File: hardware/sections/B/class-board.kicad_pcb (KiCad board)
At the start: 4 copper layers, 180 x 100 mm, 334 parts, among them J1 DevKit J1 (left row), J10 C2937625_-_Conn_01x03, J11 C2937625_-_Conn_01x03, J12 C2937625_-_Conn_01x03, J13 C492401-PZ254V-11-02P, J14 C2937625_-_Conn_01x03, J15 C2937625_-_Conn_01x03, J2 DevKit J3 (right row), J201 USB-C 16P, J202 DC005-T20, J3 C2937625_-_Conn_01x03, J4 Qwiic, J5 Expansion 2x10, J6 Panel link 2x20 female, J7 Panel link 2x20 female, J8 Panel link 2x20 female, J9 C2937625_-_Conn_01x03, J901 KF301-5.0-2P, J903 KF301-5.0-2P, J905 KF301-5.0-3P, Q901 AOD4185, Q904 AOD4184A, U101 ADS8688IDBTR, U201 LM66100DCKR, U202 LM66100DCKR, U203 78L05G-AB3-R, U204 AMS1117-3.3, U301 DAC8563SDGSR, U302 74HCT125PW, U303 OPA2192IDR, U501 SN74AHCT541PWR, U502 74HCT125PW, U503 SN74LVC1T45DBVR, U505 TCA9535PWR, U701 SI5351A-B-GT, U702 74HC74D,653, U703 OPA1656IDR, U704 DG419DY-T1-E3, U705 OPA1612AIDR, U706 OPA1612AIDR, U801 AD9834BRUZ, U802 OPA564AIDWPR, U901 TS5A23157DGSR, U902 TS5A23157DGSR, U903 DRV8871DDAR, U904 UCC27517DBVR, Y701 25 MHz

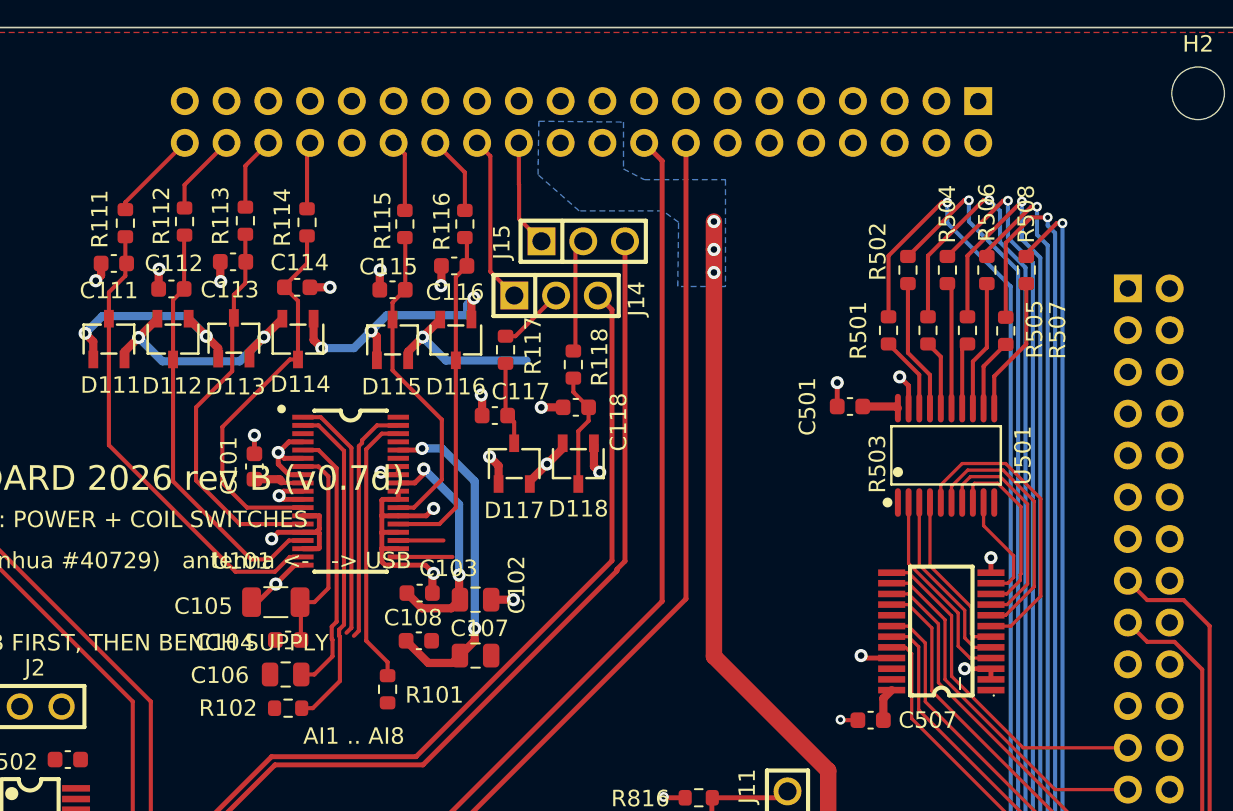
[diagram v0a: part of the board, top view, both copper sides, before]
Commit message: Merge student A (Renqian): area A of the main board (417 tracks/vias, unconnected 197 -> 148) and panel section A (13 analog nets, 121 unconnected left) accepted into the masters; sections re-split
Co-Authored-By: Claude Fable 5.1 <noreply@anthropic.com>
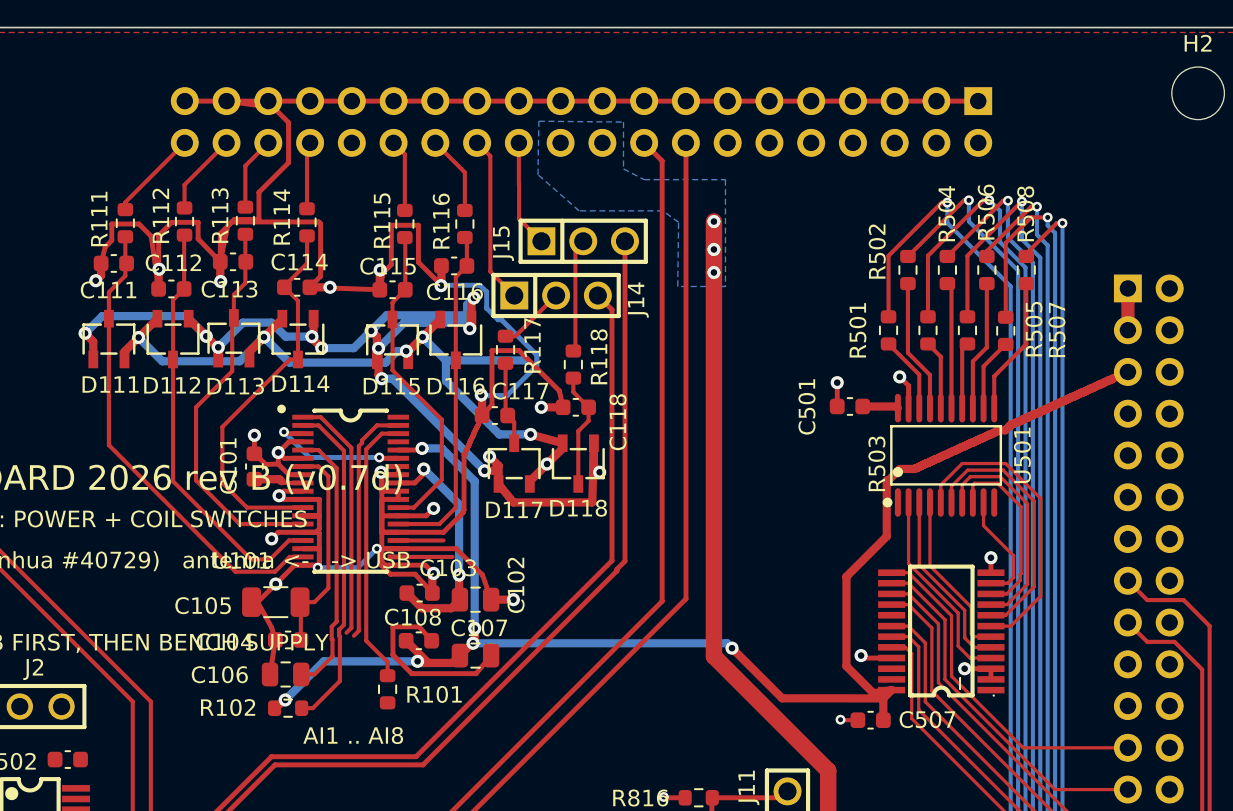
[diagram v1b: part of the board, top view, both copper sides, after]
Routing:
- net AGND: track 162.8 -> 342.1 mm, vias 87 -> 89
- net +3V3: track 77.5 -> 147.6 mm, vias 6 -> 10
- net -12V: track 80.5 -> 115.1 mm, vias 11 -> 17
- net GND: track 135.3 -> 155.5 mm, vias 68 -> 70
- net +12V: track 94.6 -> 114.1 mm, vias 9 -> 11
- net +5V_RAW: track 86.6 -> 89.1 mm

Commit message: Main board: five copper zones restored (missing from the 2026-09-24 save), student A's area-A routing accepted (26 items; 157 unconnected); Decision #70: three students on the boards (A Renqian, B Yi-Tsai, C instructor, D Lihdong) in both sections READMEs; sections re-split
Co-Authored-By: Claude Fable 5.1 <noreply@anthropic.com>
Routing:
- net AGND: track 342.1 -> 312.6 mm, vias 89 -> 87
- net +5V_RAW: track 89.1 -> 108.1 mm, vias 0 -> 3
- net /b1_inputs/CS_ADC: track 0.00 -> 10.8 mm
- net +5VA: track 34.4 -> 44.9 mm, vias 2 -> 3
- net GND: track 155.5 -> 154.3 mm, vias 70 -> 86

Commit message: Sections re-split from the instructor's 2026-09-25 masters (panel complete: 0 unconnected; main board 73 unconnected)
Co-Authored-By: Claude Fable 5.1 <noreply@anthropic.com>
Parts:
- moved J5 90.1 mm to (-62.8, 43.4)
- moved R717 90.1 mm to (-67.7, 33.8)
- moved R718 90.1 mm to (-67.8, 36.0)
- moved TP203 21.7 mm to (44.0, 78.1)
- moved C216 19.9 mm to (32.4, 65.0)
- moved C217 19.7 mm to (16.3, 65.7)
- moved FB203 19.4 mm to (37.3, 68.2)
- moved C207 19.2 mm to (38.5, 71.4)
- moved C209 19.2 mm to (36.9, 73.7)
- moved C210 19.2 mm to (37.5, 86.5)
- moved C707 19.2 mm to (43.0, 69.0)
- moved C722 19.2 mm to (44.7, 83.9)
- moved C723 19.2 mm to (15.2, 89.0)
- moved C724 19.2 mm to (44.7, 87.9)
- moved C725 19.2 mm to (11.4, 89.0)
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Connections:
- J6 pad 1: AGND -> GND
- J6 pad 10: unconnected-(J6-Pad10) -> /b1_inputs/TX
- J6 pad 11: AGND -> GND
- J6 pad 12: /b1_inputs/AUX -> /b1_inputs/TX
- J6 pad 13: AGND -> unconnected-(J6-Pad13)
- J6 pad 20: /b1_inputs/TX -> /b1_inputs/AUX
- J6 pad 22: /b1_inputs/TX -> /b1_inputs/RX
- J6 pad 3: AGND -> GND
- J6 pad 32: /b1_inputs/RX -> unconnected-(J6-Pad32)
- J6 pad 5: AGND -> GND
- J6 pad 7: AGND -> GND
- J6 pad 9: AGND -> GND
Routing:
- net /b1_inputs/AUX: track 12.2 -> 222.1 mm
- net /b1_inputs/RX: track 0.00 -> 209.7 mm
- net +5V_RAW: track 108.1 -> 291.1 mm, vias 3 -> 9
- net I2C_SDA: track 0.00 -> 155.9 mm, vias 0 -> 2
- net I2C_SCL: track 0.00 -> 150.3 mm, vias 0 -> 2
- net -12V: track 115.1 -> 259.0 mm, vias 17 -> 15
- net AGND: track 312.6 -> 174.7 mm, vias 87 -> 88
- net +VEXT: track 28.0 -> 161.4 mm, vias 0 -> 4
- net +3V3A: track 35.9 -> 146.2 mm, vias 3 -> 12
- net +5VA: track 44.9 -> 150.0 mm, vias 3 -> 6
- net +12V: track 114.1 -> 218.3 mm
- net /base_mcu/TX_EN: track 4.90 -> 101.4 mm, vias 0 -> 2
- net +3V3: track 147.6 -> 236.3 mm, vias 10 -> 11
- net /nmr_tx/+VEXT_TX: track 0.00 -> 54.3 mm
- net /b1_inputs/CS_ADC: track 10.8 -> 64.4 mm, vias 0 -> 2
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- added copper zone on F.Cu, net +VCOIL
- added copper zone on F.Cu, net /b1_inputs/TX
- added copper zone on F.Cu, net /nmr_rx/IF_QN
- added copper zone on In1.Cu, net AGND
- added copper zone on In2.Cu, net AGND
- added copper zone on B.Cu, net GND
- removed copper zone on F.Cu, net (none)
- removed copper zone on B.Cu, net /b1_inputs/TX
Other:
- board text added: "ESP32-S3-DevKitC-1 (Jinhua #40729)"
- board text removed: "ESP32-S3-DevKitC-1 (Jinhua #40729) antenna <- -> USB"
- board text removed: "INSTRUCTOR: POWER + COIL SWITCHES"
- board text removed: "J7 PANEL LINK pin 1 ->"
- board text removed: "J8 PANEL LINK pin 1 ->"
